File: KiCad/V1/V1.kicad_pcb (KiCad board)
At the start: 4 copper layers, 130.8 x 93.1 mm, 84 parts, among them Q1 Q_NMOS_GSD, Q2 Q_NMOS_GSD, U1 LMG1210RVRR, U2 OPA2677IDDA, U3 OPA2677IDDA, U4 OPA859QDSGRQ1, U5 OPA859QDSGRQ1, U6 OPA859QDSGRQ1

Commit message: V1 done
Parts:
- removed EN1: MountingHole_Pad, TestPoint:TestPoint_THTPad_D2.5mm_Drill1.2mm
- removed PWM_IN1, Pre_Filter2, Pre_Filter3, Pre_Filter4: Conn_Coaxial, Connector_Coaxial:U.FL_Molex_MCRF_73412-0110_Vertical
- added EN1_coax1: Conn_Coaxial, Connector_Coaxial:U.FL_Molex_MCRF_73412-0110_Vertical, B.Cu at (118.5, 61.5)
- added PWM_External1: Conn_Coaxial, Connector_Coaxial:U.FL_Molex_MCRF_73412-0110_Vertical, B.Cu at (109.9, 61.5)
- added Pre_FilterV_ref1: Conn_Coaxial, Connector_Coaxial:U.FL_Molex_MCRF_73412-0110_Vertical, B.Cu at (132.0, 61.5)
- added T1: Transformer_1P_1S, MyFootprints:MyTransformer, B.Cu at (159.8, 51.1)
- added V_duffsense1: Conn_Coaxial, Connector_Coaxial:U.FL_Molex_MCRF_73412-0110_Vertical, B.Cu at (125.7, 61.5)
- moved H5 94.0 mm to (177.9, 25.6)
- moved H7 84.9 mm to (177.9, 69.6)
- moved R12 36.7 mm to (165.9, 61.5), turned to 90 degrees
- moved C13 36.0 mm to (166.0, 59.1), turned to 90 degrees
- moved Post_Filter1 31.7 mm to (162.2, 61.4), turned to -90 degrees
- moved H6 25.2 mm to (92.9, 69.6)
- moved VDD_PWM_BIG2 12.8 mm to (179.1, 45.4)
- moved VDD_PWM_BIG3 12.8 mm to (179.1, 55.3)
- moved H8 10.8 mm to (92.9, 25.6)
- moved R_shutn1 8.90 mm to (159.7, 52.8), turned to 180 degrees
- moved C24 1.62 mm to (156.3, 60.0)
- moved C25 1.62 mm to (155.7, 62.8)
- moved C26 1.62 mm to (155.7, 61.5)
- moved RdtL1 0.45 mm to (118.0, 42.5)
- moved C3 0.34 mm to (120.7, 42.5)
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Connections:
- C13 pad 2: /OUT -> /+I_OUT
- Q1 pad 3: /VDD_PWM_Big -> /HS1
- Q1 pad 4: (no net) -> /VDD_PWM_Big
- Q1 pad 5: (no net) -> /HS1
- Q1 pad 6: (no net) -> /HS1
- Q2 pad 3: /HS1 -> GND
- Q2 pad 4: (no net) -> /HS1
- Q2 pad 5: (no net) -> GND
- Q2 pad 6: (no net) -> GND
- VDD_PWM_BIG3 pad 1: /-I_OUT -> GND
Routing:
- net /+I_OUT: track 0.00 -> 31.8 mm
- net Net-(T1-SA): track 10.2 -> 29.8 mm, vias 0 -> 2
- net /EN1: track 44.0 -> 30.6 mm
- net Net-(T1-AB): track 17.5 -> 9.86 mm
- net Net-(T1-SB): track 8.17 -> 13.1 mm
- net /PWM_External: track 0.08 -> 4.26 mm, vias 1 -> 2
- net Net-(C13-Pad1): track 0.00 -> 1.41 mm
- net GND: track 19.2 -> 20.3 mm, vias 53 -> 531
- net Net-(U1-PWM/LI): track 28.7 -> 29.7 mm
- net Net-(U1-DHL): track 4.12 -> 5.11 mm
- net /VDD10: track 21.8 -> 21.1 mm
- net Net-(C1-Pad1): track 7.22 -> 6.96 mm, vias 0 -> 1
- net /VDD_PWM_Big: vias 14 -> 16
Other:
- board size 130.8 x 93.1 mm -> 98 x 55.2 mm
- board text added: "+10V"
- board text added: "+2V"
- board text added: "+5V"
- board text added: "-2V"
- board text added: "I_Out"

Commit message: Fixed GanfetPad clerance
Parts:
- C17: footprint Capacitor_SMD:C_0402_1005Metric -> Capacitor_SMD:C_0805_2012Metric
- moved C17 1.77 mm to (130.9, 45.8), turned to -90 degrees
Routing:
- net GND: vias 531 -> 66
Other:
- board text added: "Designed by David Kwiatkowski"

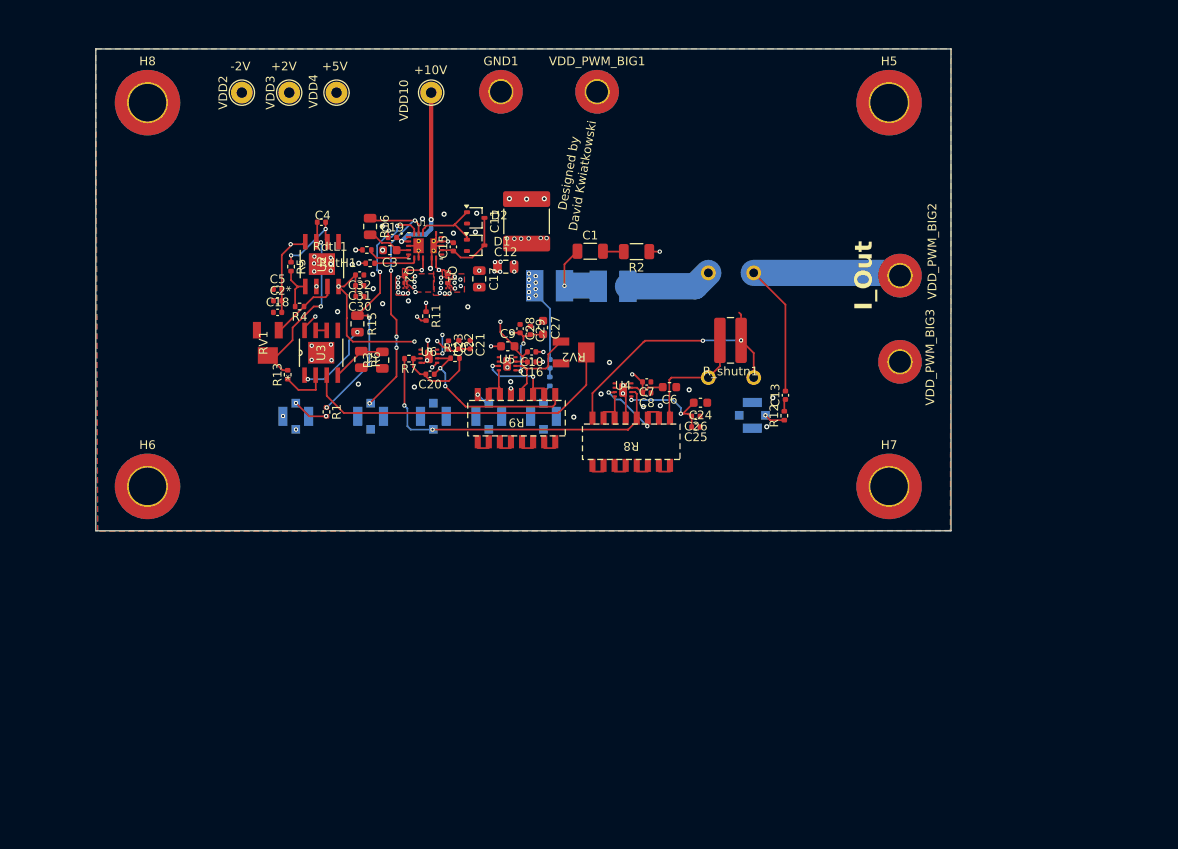
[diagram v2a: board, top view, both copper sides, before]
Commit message: Borgs pcb via addition
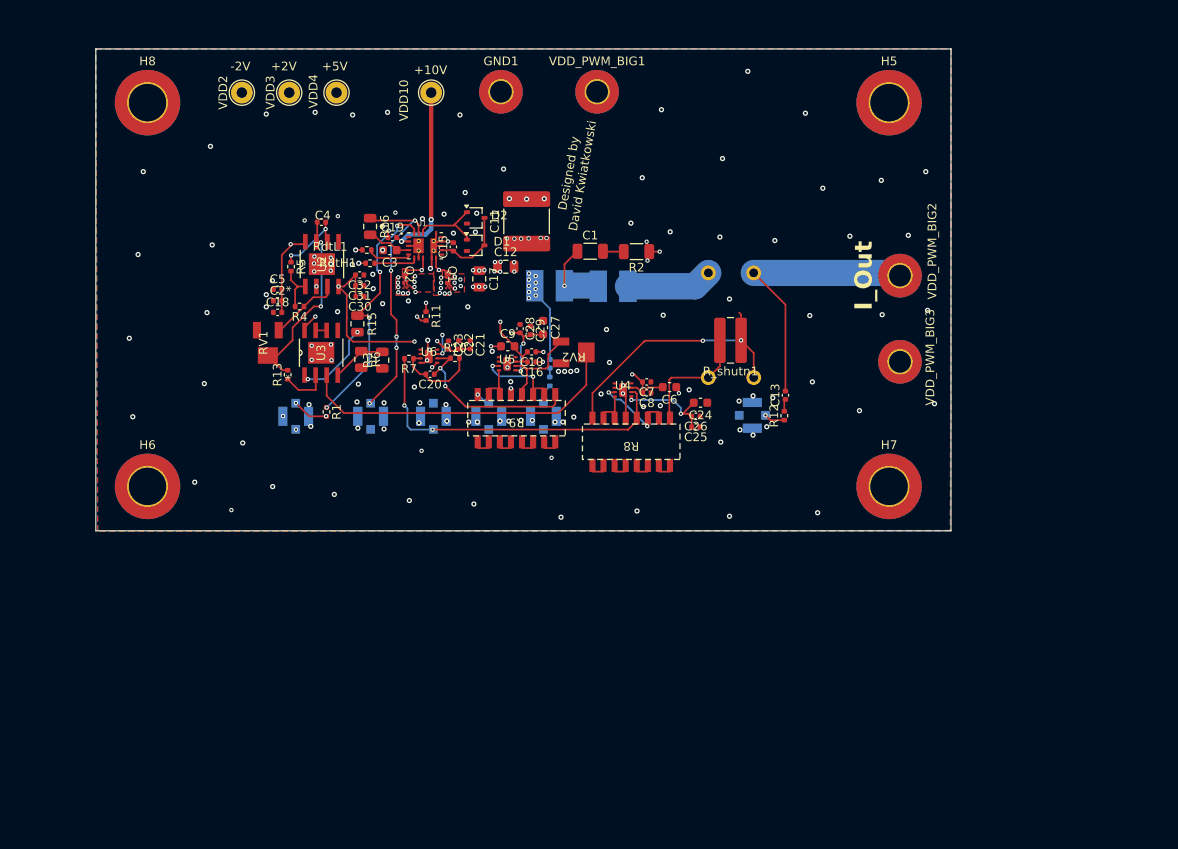
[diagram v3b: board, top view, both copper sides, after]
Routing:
- net GND: vias 66 -> 156
- net /VDD_PWM_Big: vias 16 -> 18
